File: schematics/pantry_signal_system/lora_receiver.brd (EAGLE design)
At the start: 39.4 x 61.9 mm, 6 parts, among them J1 JST-XH254-2P, U1 ESP32, U12 E220-900T22D, U2 SN74LVC2T45DCUR, U3 SN74LVC2T45DCUR

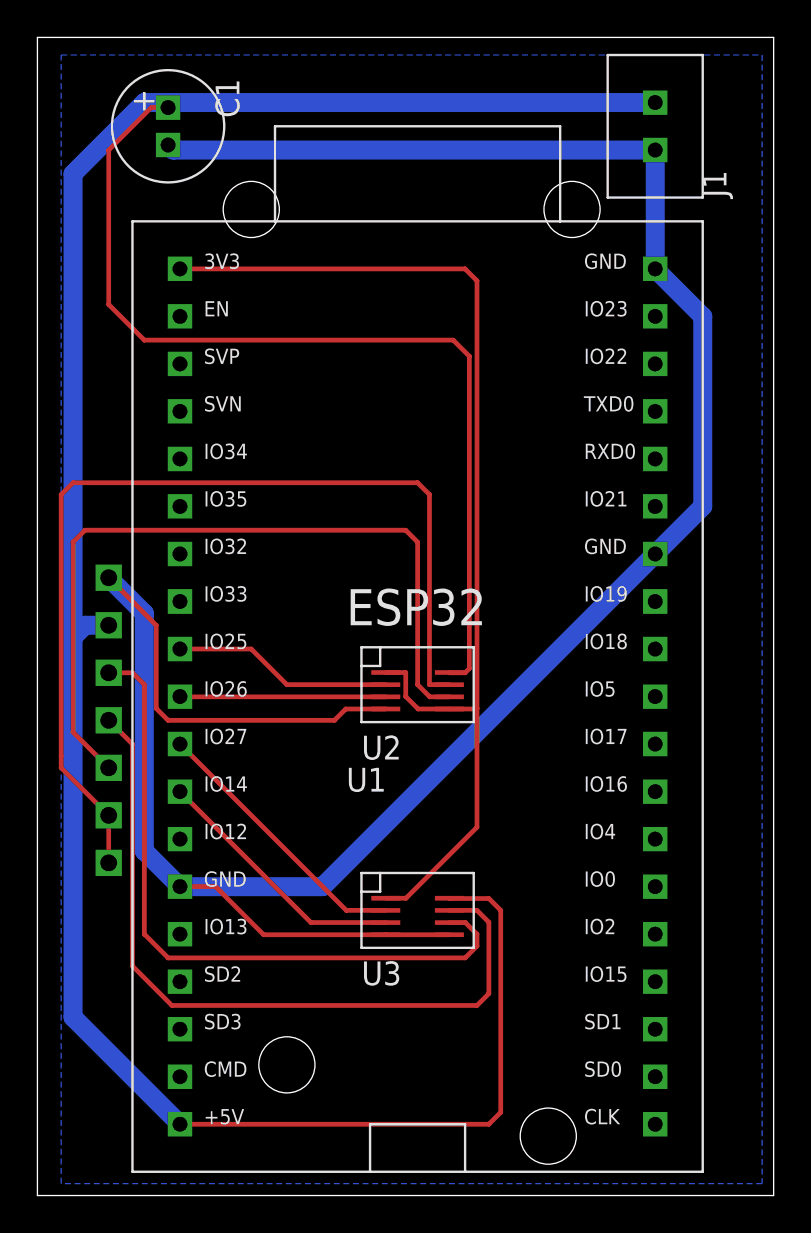
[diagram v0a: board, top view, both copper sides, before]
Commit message: Changes in schematics, changes in source code. Current version works too, but I changed boards to fix some possible errors
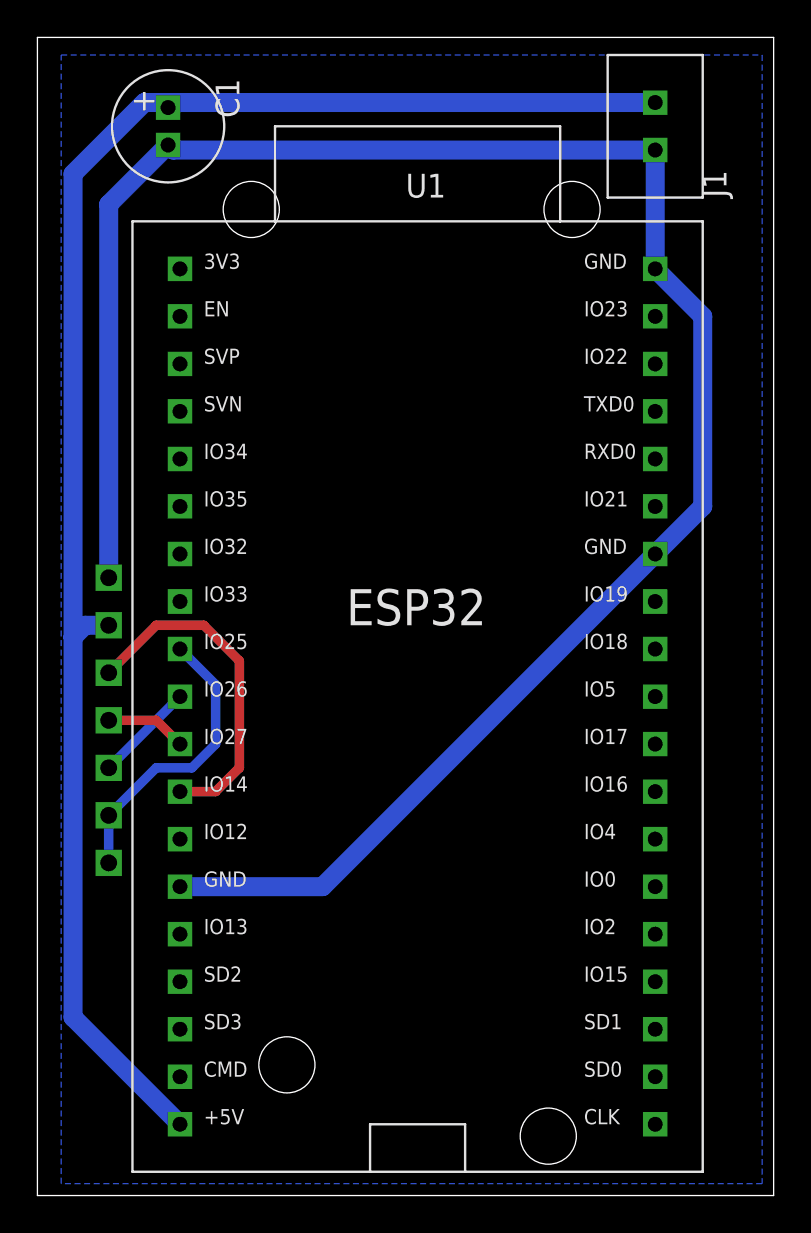
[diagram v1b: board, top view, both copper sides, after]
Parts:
- removed U2, U3: SN74LVC2T45DCUR, my_devices:VSSOP-8
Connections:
- removed net N$1: U12.TX, U3.P7
- removed net N$2: U12.RX, U2.P6
- removed net N$3: U12.AUX, U3.P6
- removed net N$9: U12.M0, U12.M1, U2.P7
- net +5V: no longer U2.P8, U3.P8
- net 3V3: no longer U2.P1, U2.P5, U3.P1
- net GND: no longer U2.P4, U3.P4, U3.P5
- net LORA_AUX: now also U12.AUX; no longer U3.P3
- net LORA_M0M1: now also U12.M0, U12.M1; no longer U2.P2
- net LORA_RX: now also U12.RX; no longer U2.P3
- net LORA_TX: now also U12.TX; no longer U3.P2
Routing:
- net +5V: track 170.3 -> 88.4 mm
- net 3V3: track 58.2 -> 0.00 mm
- net N$9: track 52.2 -> 0.00 mm
- net N$2: track 41.4 -> 0.00 mm
- net N$1: track 40.0 -> 0.00 mm
- net N$3: track 36.4 -> 0.00 mm
- net GND: track 137.0 -> 107.1 mm
- net LORA_TX: track 14.7 -> 4.34 mm
- net LORA_RX: track 11.0 -> 5.39 mm
- net LORA_AUX: track 13.9 -> 18.2 mm
- net LORA_M0M1: track 11.8 -> 15.7 mm

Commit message: Debugging logic module firmware, estabilishing LoRa connection....
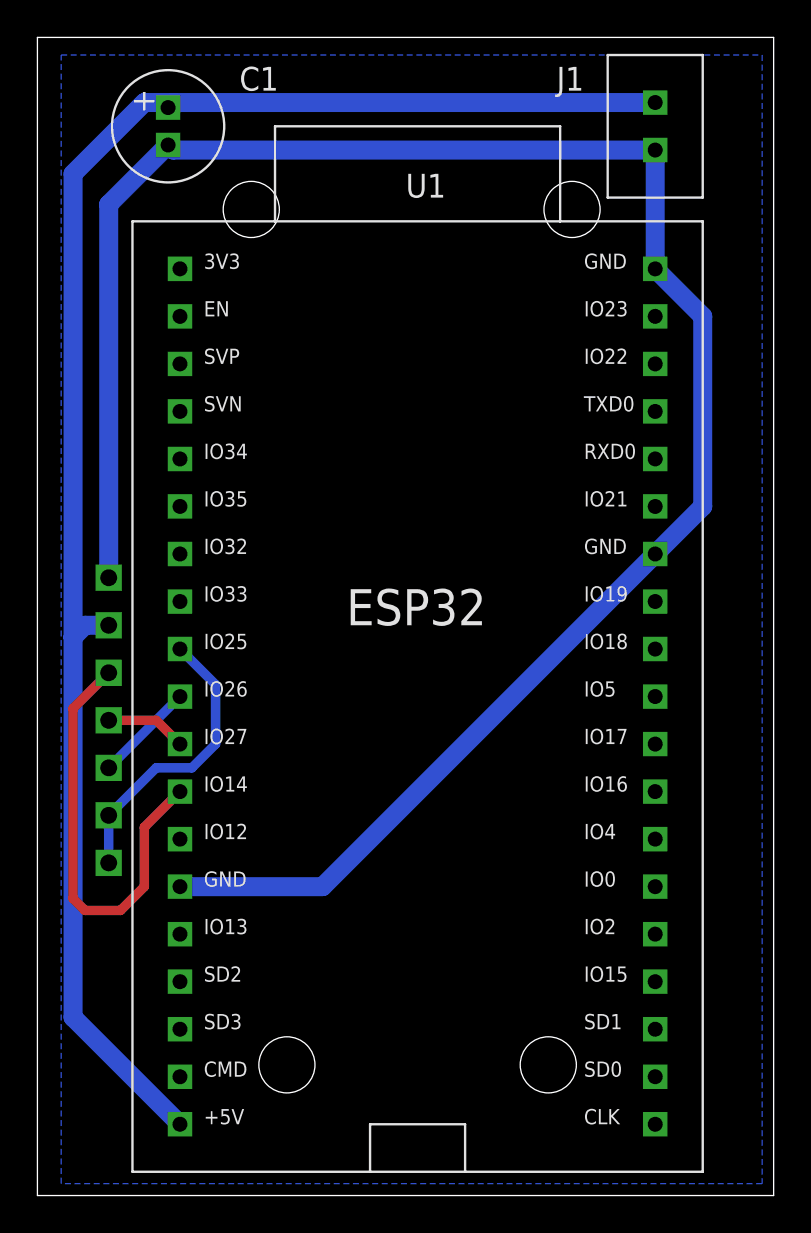
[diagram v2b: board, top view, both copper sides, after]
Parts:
- renumbered U12 to U2
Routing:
- net LORA_AUX: track 18.2 -> 23.3 mm
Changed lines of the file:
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@@
 <drawing>
 <settings>
-<setting alwaysvectorfont="no"/>
+<setting alwaysvectorfont="yes"/>
 <setting verticaltext="up"/>
 </settings>
@@
 <text x="82.55" y="85.09" size="1.778" layer="26" rot="MR0">GND</text>
 <hole x="56.515" y="37.465" drill="3"/>
-<hole x="70.485" y="33.655" drill="3"/>
+<hole x="70.485" y="37.465" drill="3"/>
 <hole x="54.61" y="83.185" drill="3"/>
 <hole x="71.755" y="83.185" drill="3"/>
@@
 <elements>
 <element name="J1" library="my_devices" package="JST-XH254-2P" value="JST-XH254-2P" x="76.2" y="87.63" smashed="yes" rot="R90">
-<attribute name="NAME" x="80.01" y="83.82" size="1.27" layer="21" rot="R90"/>
+<attribute name="NAME" x="72.39" y="90.805" size="1.27" layer="21" rot="R180"/>
 </element>
 <element name="U1" library="my_devices" package="ESP32" value="ESP32" x="63.5" y="57.15" smashed="yes">
 <attribute name="NAME" x="62.865" y="83.82" size="1.27" layer="21"/>
 </element>
-<element name="U12" library="my_devices" package="LORA" value="E220-900T22D" x="63.5" y="55.88" smashed="yes" rot="MR0">
+<element name="U2" library="my_devices" package="LORA" value="E220-900T22D" x="63.5" y="55.88" smashed="yes" rot="MR0">
 <attribute name="NAME" x="66.04" y="58.42" size="1.27" layer="22" rot="MR0"/>
 </element>
 <element name="C1" library="my_devices" package="C-MINI-5X7" value="10 uF" x="50.165" y="87.63" smashed="yes" rot="R270">
-<attribute name="NAME" x="52.705" y="90.17" size="1.27" layer="21" rot="R270"/>
+<attribute name="NAME" x="53.975" y="89.535" size="1.27" layer="21"/>
 </element>
 </elements>
@@
 <contactref element="U1" pad="GND_1"/>
 <contactref element="U1" pad="GND"/>
-<contactref element="U12" pad="GND"/>
+<contactref element="U2" pad="GND"/>
 <wire x1="76.2" y1="80.01" x2="78.74" y2="77.47" width="1.016" layer="16"/>
 <wire x1="78.74" y1="77.47" x2="78.74" y2="67.31" width="1.016" layer="16"/>
@@
 <contactref element="U1" pad="+5V"/>
 <contactref element="J1" pad="PIN2"/>
-<contactref element="U12" pad="VCC"/>
+<contactref element="U2" pad="VCC"/>
 <wire x1="50.8" y1="34.29" x2="45.085" y2="40.005" width="1.016" layer="16"/>
 <contactref element="C1" pad="PLUS"/>
@@
 <signal name="LORA_RX">
 <contactref element="U1" pad="IO26"/>
-<contactref element="U12" pad="RX"/>
+<contactref element="U2" pad="RX"/>
 <wire x1="46.99" y1="53.34" x2="50.8" y2="57.15" width="0.508" layer="16"/>
 </signal>
 <signal name="LORA_TX">
 <contactref element="U1" pad="IO27"/>
-<contactref element="U12" pad="TX"/>
+<contactref element="U2" pad="TX"/>
 <wire x1="46.99" y1="55.88" x2="49.53" y2="55.88" width="0.508" layer="1"/>
 <wire x1="49.53" y1="55.88" x2="50.8" y2="54.61" width="0.508" layer="1"/>
@@
 <signal name="LORA_AUX">
 <contactref element="U1" pad="IO14"/>
-<contactref element="U12" pad="AUX"/>
-<wire x1="46.99" y1="58.42" x2="49.53" y2="60.96" width="0.508" layer="1"/>
-<wire x1="49.53" y1="60.96" x2="52.07" y2="60.96" width="0.508" layer="1"/>
-<wire x1="52.07" y1="60.96" x2="53.975" y2="59.055" width="0.508" layer="1"/>
-<wire x1="53.975" y1="53.34" x2="52.705" y2="52.07" width="0.508" layer="1"/>
-<wire x1="52.705" y1="52.07" x2="50.8" y2="52.07" width="0.508" layer="1"/>
-<wire x1="53.975" y1="59.055" x2="53.975" y2="53.34" width="0.508" layer="1"/>
+<contactref element="U2" pad="AUX"/>
+<wire x1="46.99" y1="58.42" x2="45.085" y2="56.515" width="0.508" layer="1"/>
+<wire x1="45.085" y1="46.355" x2="45.72" y2="45.72" width="0.508" layer="1"/>
+<wire x1="45.72" y1="45.72" x2="47.625" y2="45.72" width="0.508" layer="1"/>
+<wire x1="47.625" y1="45.72" x2="48.895" y2="46.99" width="0.508" layer="1"/>
+<wire x1="48.895" y1="50.165" x2="50.8" y2="52.07" width="0.508" layer="1"/>
+<wire x1="45.085" y1="56.515" x2="45.085" y2="46.355" width="0.508" layer="1"/>
+<wire x1="48.895" y1="46.99" x2="48.895" y2="50.165" width="0.508" layer="1"/>
 </signal>
 <signal name="LORA_M0M1">
 <contactref element="U1" pad="IO25"/>
-<contactref element="U12" pad="M1"/>
-<contactref element="U12" pad="M0"/>
+<contactref element="U2" pad="M1"/>
+<contactref element="U2" pad="M0"/>
 <wire x1="50.8" y1="59.69" x2="52.705" y2="57.785" width="0.508" layer="16"/>
 <wire x1="52.705" y1="57.785" x2="52.705" y2="54.61" width="0.508" layer="16"/>
